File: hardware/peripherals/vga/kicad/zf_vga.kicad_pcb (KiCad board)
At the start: 2 copper layers, 33 parts, among them J2 Conn_02x13_Odd_Even, J3 DB15_Female, J4 DB9_Male, J5 DB9_Male, SW1 SW_DIP_x03, U1 4040, U10 74HC165, U11 AS6C6264, U12 74HC541, U13 74HC541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

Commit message: Bypass caps
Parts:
- added C10: 0.1uF, Capacitor_THT:C_Disc_D7.5mm_W2.5mm_P5.00mm, F.Cu at (149.9, 116.8)
- added C11: 0.1uF, Capacitor_THT:C_Disc_D7.5mm_W2.5mm_P5.00mm, F.Cu at (162.6, 82.5)
- added C12: 0.1uF, Capacitor_THT:C_Disc_D7.5mm_W2.5mm_P5.00mm, F.Cu at (149.9, 82.5)
- added C13: 0.1uF, Capacitor_THT:C_Disc_D7.5mm_W2.5mm_P5.00mm, F.Cu at (137.2, 74.9)
- added C14: 0.1uF, Capacitor_THT:C_Disc_D7.5mm_W2.5mm_P5.00mm, F.Cu at (124.5, 116.8)
- added C15: 0.1uF, Capacitor_THT:C_Disc_D7.5mm_W2.5mm_P5.00mm, F.Cu at (111.8, 116.8)
- added C16: 0.1uF, Capacitor_THT:C_Disc_D7.5mm_W2.5mm_P5.00mm, F.Cu at (104.1, 92.7)
- added C17: 0.1uF, Capacitor_THT:C_Disc_D7.5mm_W2.5mm_P5.00mm, F.Cu at (120.7, 92.7)
- added C18: 0.1uF, Capacitor_THT:C_Disc_D7.5mm_W2.5mm_P5.00mm, F.Cu at (200.7, 82.5)
- added C19: 0.1uF, Capacitor_THT:C_Disc_D7.5mm_W2.5mm_P5.00mm, F.Cu at (188.0, 82.5)
- added C20: 0.1uF, Capacitor_THT:C_Disc_D7.5mm_W2.5mm_P5.00mm, F.Cu at (175.3, 82.5)
- added C6: 0.1uF, Capacitor_THT:C_Disc_D7.5mm_W2.5mm_P5.00mm, F.Cu at (201.9, 116.8)
- added C7: 0.1uF, Capacitor_THT:C_Disc_D7.5mm_W2.5mm_P5.00mm, F.Cu at (188.0, 116.8)
- added C8: 0.1uF, Capacitor_THT:C_Disc_D7.5mm_W2.5mm_P5.00mm, F.Cu at (162.6, 116.8)
- added C9: 0.1uF, Capacitor_THT:C_Disc_D7.5mm_W2.5mm_P5.00mm, F.Cu at (175.3, 116.8)
- SW1: footprint Button_Switch_THT:SW_DIP_SPSTx03_Slide_6.7x9.18mm_W7.62mm_P2.54mm_LowProfile -> Package_DIP:DIP-6_W7.62mm_LongPads
- U1, U10, U2: footprint Package_DIP:DIP-16_W7.62mm -> Package_DIP:DIP-16_W7.62mm_LongPads
- U11: footprint Package_DIP:DIP-28_W15.24mm -> Package_DIP:DIP-28_W15.24mm_LongPads
- U12, U13, U14, U3, U4, U5, U6: footprint Package_DIP:DIP-20_W7.62mm -> Package_DIP:DIP-20_W7.62mm_LongPads
- U7, U8, U9: footprint Package_DIP:DIP-14_W7.62mm -> Package_DIP:DIP-14_W7.62mm_LongPads
- X1: footprint Oscillator:Oscillator_DIP-14 -> Oscillator:Oscillator_DIP-14_LargePads
- moved U7 59.2 mm to (143.5, 71.1)
- moved U2 47.1 mm to (168.9, 113.0)
- moved C1 45.0 mm to (142.2, 116.8)
- moved C2 44.7 mm to (142.2, 110.5)
- moved C3 44.7 mm to (142.2, 105.4)
- moved R1 43.7 mm to (143.5, 100.3)
- moved R2 43.4 mm to (143.5, 95.2)
- moved R3 43.4 mm to (143.5, 90.2)
- moved J4 38.3 mm to (154.9, 123.2)
- moved J5 37.0 mm to (189.2, 123.2)
- moved C4 36.4 mm to (91.4, 81.3), turned to 0 degrees
- moved U1 34.5 mm to (194.3, 113.0)
- moved R7 32.5 mm to (97.8, 86.4), turned to 180 degrees
- moved U9 29.5 mm to (118.1, 113.0)
- moved U8 29.2 mm to (130.8, 113.0)
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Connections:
- C4 pad 1: GND -> Net-(C4-Pad1)
- C4 pad 2: Net-(C4-Pad2) -> GND
- C5 pad 1: GND -> Net-(C5-Pad1)
- C5 pad 2: Net-(C4-Pad2) -> GND
- J3 pad 13: Net-(J3-Pad13) -> Net-(C4-Pad1)
- J3 pad 14: Net-(C4-Pad2) -> Net-(C5-Pad1)
- R7 pad 2: Net-(J3-Pad13) -> Net-(C4-Pad1)
- R8 pad 2: Net-(C4-Pad2) -> Net-(C5-Pad1)
- U12 pad 11: D7 -> D0
- U12 pad 12: D6 -> D1
- U12 pad 13: D5 -> D2
- U12 pad 14: D4 -> D3
- U12 pad 15: D3 -> D4
- U12 pad 16: D2 -> D5
- U12 pad 17: D1 -> D6
- U12 pad 18: D0 -> D7
- U12 pad 2: PA0 -> PA7
- U12 pad 3: PA1 -> PA6
- U12 pad 4: PA2 -> PA5
- U12 pad 5: PA3 -> PA4
- U12 pad 6: PA4 -> PA3
- U12 pad 7: PA5 -> PA2
- U12 pad 8: PA6 -> PA1
- U12 pad 9: PA7 -> PA0
- U13 pad 11: A7 -> A0
- U13 pad 12: A6 -> A1
- U13 pad 13: A5 -> A2
- U13 pad 14: A4 -> A3
- U13 pad 15: A3 -> A4
- U13 pad 16: A2 -> A5
- U13 pad 17: A1 -> A6
- U13 pad 18: A0 -> A7
- U13 pad 2: PB0 -> PB7
- U13 pad 3: PB1 -> PB6
- U13 pad 4: PB2 -> PB5
- U13 pad 5: PB3 -> PB4
- U13 pad 6: PB4 -> PB3
- U13 pad 7: PB5 -> PB2
- U13 pad 8: PB6 -> PB1
- U13 pad 9: PB7 -> PB0
- U14 pad 16: A10 -> A8
- U14 pad 18: A8 -> A10
- U14 pad 2: PC0 -> PC2
- U14 pad 4: PC2 -> PC0
- U3 pad 1: P0 -> P9
- U3 pad 11: P9 -> P0
- U3 pad 2: P1 -> P8
- U3 pad 3: P2 -> P7
- U3 pad 4: P3 -> P6
- U3 pad 5: P4 -> P5
- U3 pad 6: P5 -> P4
- U3 pad 7: P6 -> P3
- U3 pad 8: P7 -> P2
- U3 pad 9: P8 -> P1
- U4 pad 1: L0 -> L9
- U4 pad 11: L9 -> L0
- U4 pad 2: L1 -> L8
- U4 pad 3: L2 -> L7
- U4 pad 4: L3 -> L6
- U4 pad 5: L4 -> L5
- U4 pad 6: L5 -> L4
- U4 pad 7: L6 -> L3
- U4 pad 8: L7 -> L2
- U4 pad 9: L8 -> L1
- U5 pad 15: A3 -> A0
- U5 pad 16: A2 -> A1
- U5 pad 17: A1 -> A2
- U5 pad 18: A0 -> A3
- U5 pad 2: P5 -> P8
- U5 pad 3: P6 -> P7
- U5 pad 4: P7 -> P6
- U5 pad 5: P8 -> P5
- U6 pad 12: A10 -> A4
- U6 pad 13: A9 -> A5
- U6 pad 14: A8 -> A6
- U6 pad 16: A6 -> A8
- U6 pad 17: A5 -> A9
- U6 pad 18: A4 -> A10
- U6 pad 2: L2 -> L8
- U6 pad 3: L3 -> L7
- U6 pad 4: L4 -> L6
- U6 pad 6: L6 -> L4
- U6 pad 7: L7 -> L3
- U6 pad 8: L8 -> L2

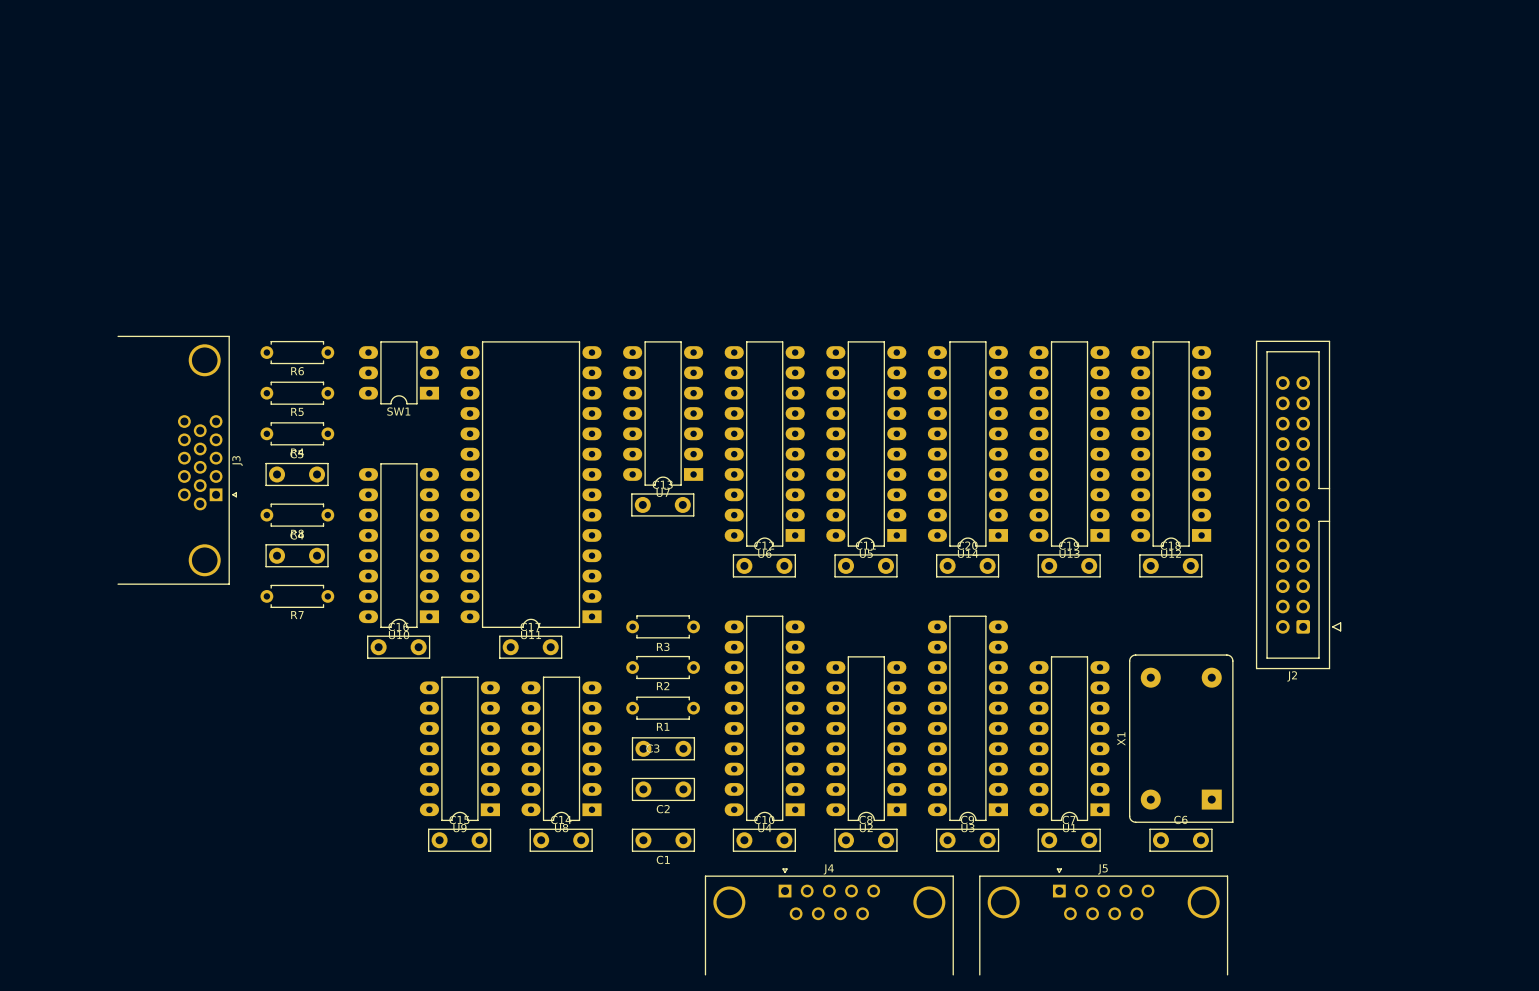
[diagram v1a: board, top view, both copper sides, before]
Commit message: Expansion port footprint
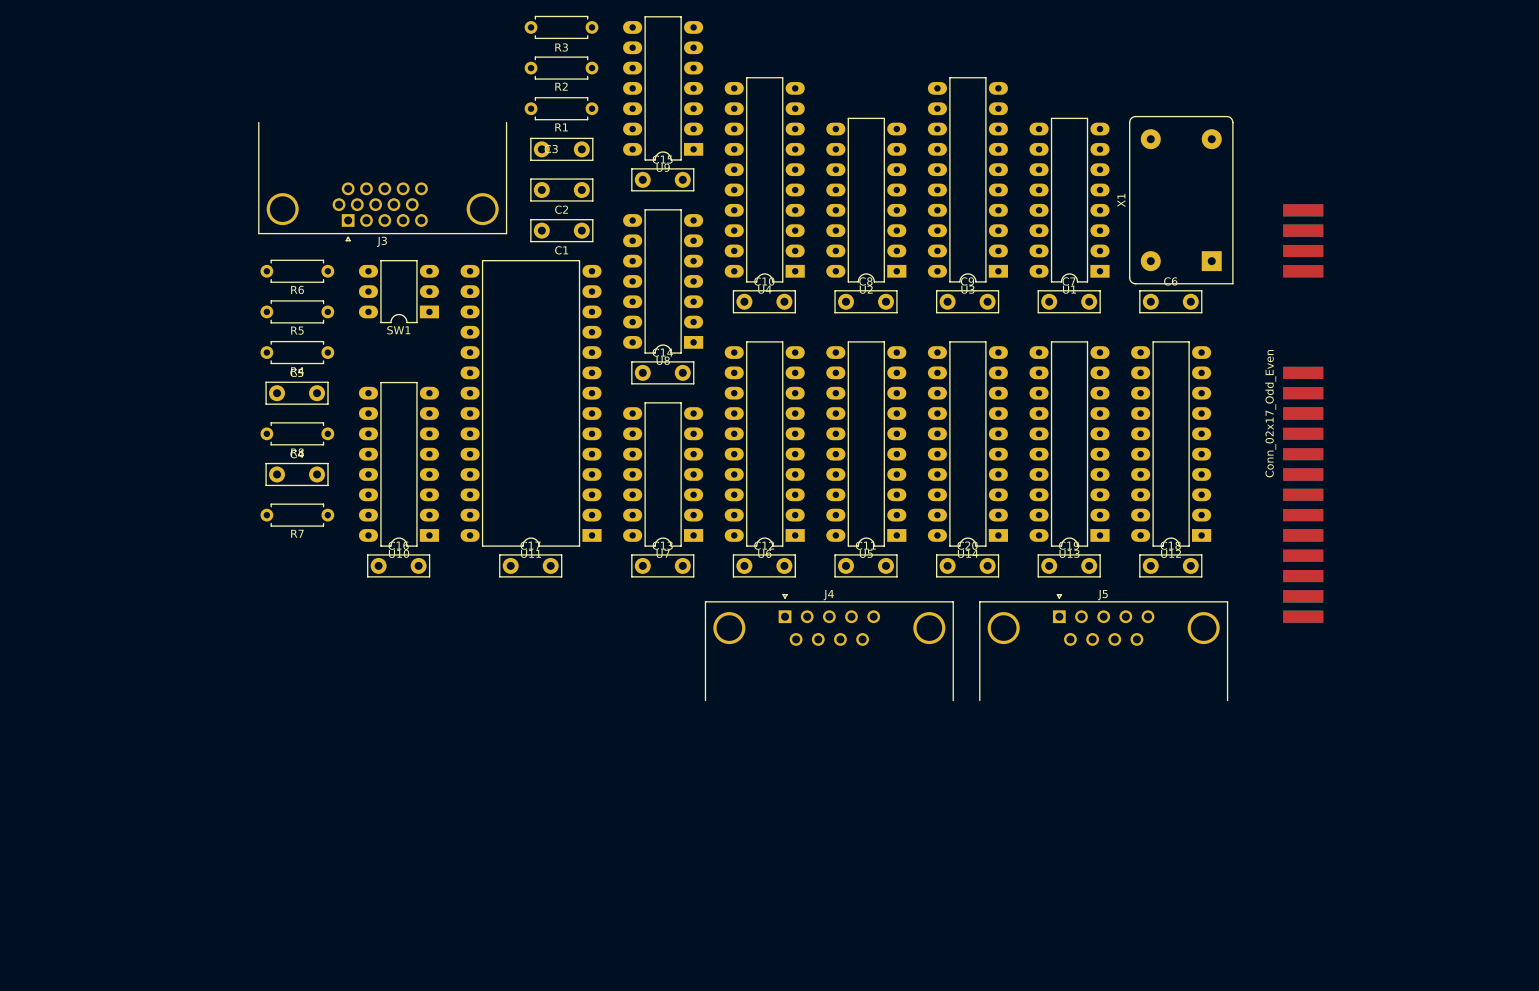
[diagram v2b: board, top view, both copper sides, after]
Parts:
- J2: value Conn_02x13_Odd_Even -> Conn_02x17_Odd_Even; footprint Connector_IDC:IDC-Header_2x13_P2.54mm_Vertical -> Z-FIGHTER:Z-FIGHTER_Expansion_Port
- moved C15 86.4 mm to (137.2, 34.3)
- moved U9 86.4 mm to (143.5, 30.5)
- moved C1 77.3 mm to (129.5, 40.6)
- moved C2 76.0 mm to (129.5, 35.6)
- moved C3 76.0 mm to (129.5, 30.5)
- moved R1 76.0 mm to (130.8, 25.4)
- moved R2 76.0 mm to (130.8, 20.3)
- moved R3 76.0 mm to (130.8, 15.2)
- moved C6 67.3 mm to (200.7, 49.5)
- moved C10 67.3 mm to (149.9, 49.5)
- moved C7 67.3 mm to (188.0, 49.5)
- moved C8 67.3 mm to (162.6, 49.5)
- moved C9 67.3 mm to (175.3, 49.5)
- moved U1 67.3 mm to (194.3, 45.7)
- moved U2 67.3 mm to (168.9, 45.7)
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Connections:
- net Net-(SW1-Pad1) renamed VIDOUT

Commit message: Board layout progress
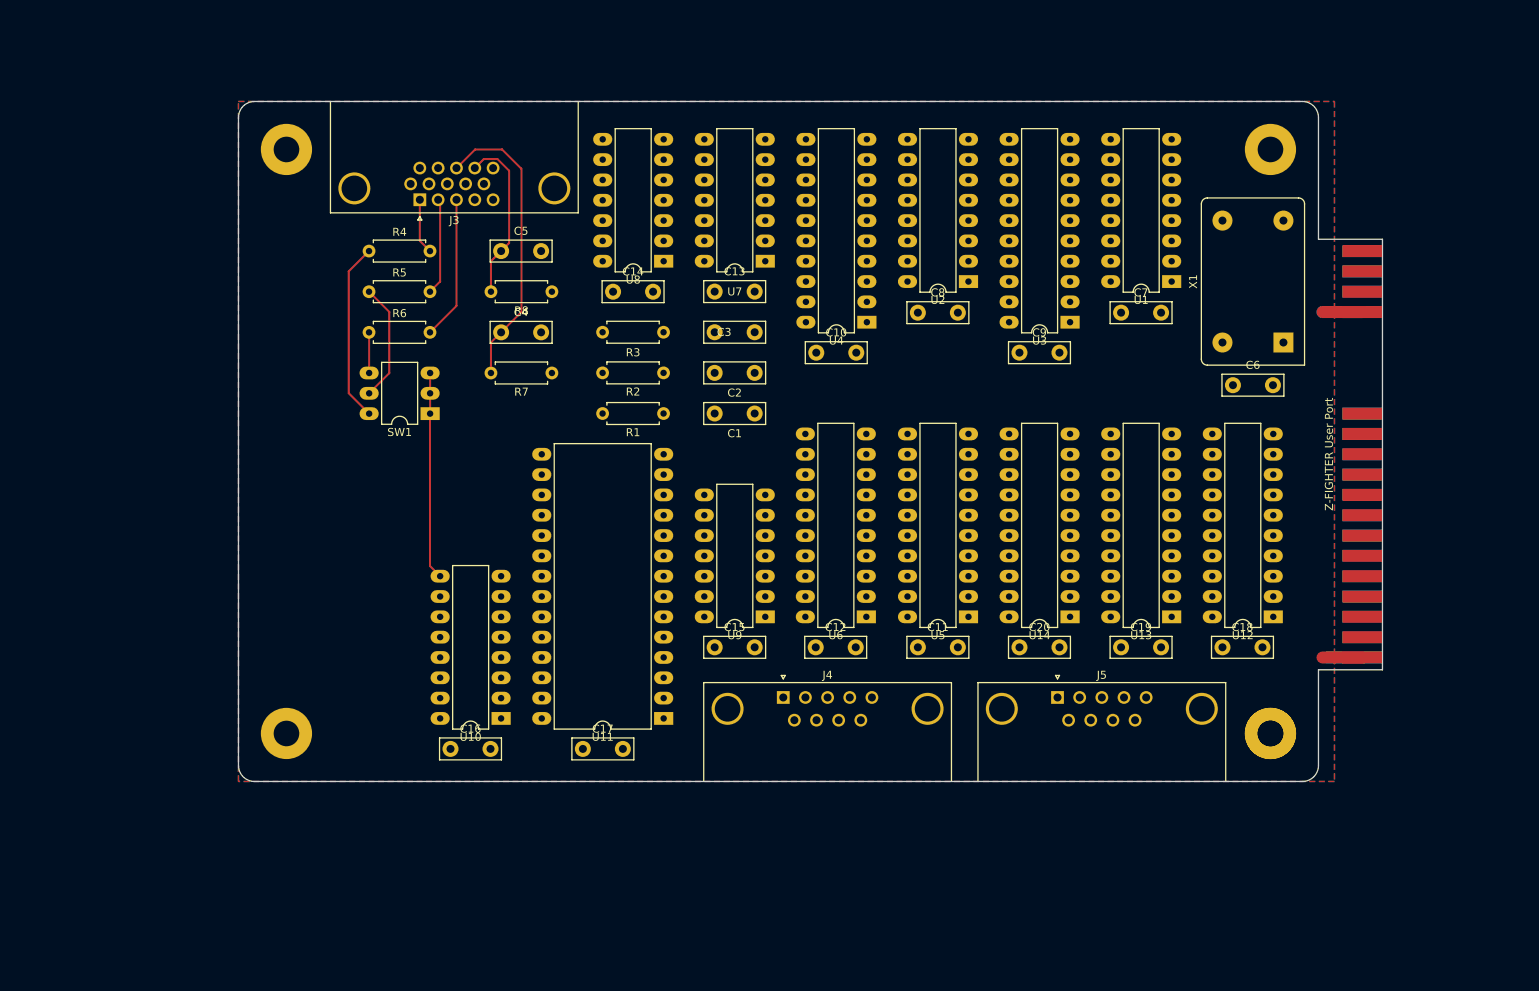
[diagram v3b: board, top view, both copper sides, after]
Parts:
- added Mount1: MountingHole_3.2mm_M3_Pad, MountingHole:MountingHole_3.2mm_M3_Pad, F.Cu at (92.6, 30.5)
- added Mount1: MountingHole_3.2mm_M3_Pad, MountingHole:MountingHole_3.2mm_M3_Pad, F.Cu at (215.6, 30.5)
- added Mount3: MountingHole_3.2mm_M3_Pad, MountingHole:MountingHole_3.2mm_M3_Pad, F.Cu at (92.6, 103.5)
- added Mount4 (x2): MountingHole_3.2mm_M3_Pad, MountingHole:MountingHole_3.2mm_M3_Pad, F.Cu at (215.6, 103.5)
- J2: value Conn_02x17_Odd_Even -> Z-FIGHTER User Port
- moved C15 59.1 mm to (146.1, 92.7)
- moved U9 59.1 mm to (152.5, 88.9)
- moved R1 39.1 mm to (139.8, 63.5)
- moved R2 39.1 mm to (139.8, 58.4)
- moved R3 39.1 mm to (139.8, 53.3)
- moved C13 35.4 mm to (146.1, 48.3)
- moved U7 35.4 mm to (152.5, 44.5)
- moved C4 33.2 mm to (119.4, 53.4)
- moved C5 33.2 mm to (119.4, 43.2)
- moved R7 33.2 mm to (125.8, 58.4)
- moved R8 33.2 mm to (125.8, 48.3)
- moved C1 31.5 mm to (151.1, 63.5)
- moved C2 31.5 mm to (151.1, 58.4)
- moved C3 31.5 mm to (151.1, 53.3)
- moved C17 24.6 mm to (129.7, 105.4)
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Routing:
- net Net-(C4-Pad1): track 0.00 -> 37.2 mm
- net VIDOUT: track 0.00 -> 25.9 mm
- net Net-(R4-Pad1): track 0.00 -> 22.4 mm
- net Net-(C5-Pad1): track 0.00 -> 21.4 mm
- net Net-(J3-Pad3): track 0.00 -> 17.9 mm
- net Net-(R5-Pad1): track 0.00 -> 14.8 mm
- net Net-(J3-Pad2): track 0.00 -> 12.1 mm
- net GND: track 0.00 -> 10.0 mm
- net VCC: track 0.00 -> 9.50 mm
- net Net-(J3-Pad1): track 0.00 -> 6.94 mm
- net Net-(R6-Pad1): track 0.00 -> 5.09 mm
- added copper zone on F.Cu, net GND
- added copper zone on B.Cu, net VCC
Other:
- board outline added: 143 x 85 mm

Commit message: Connected #RESET from ZF
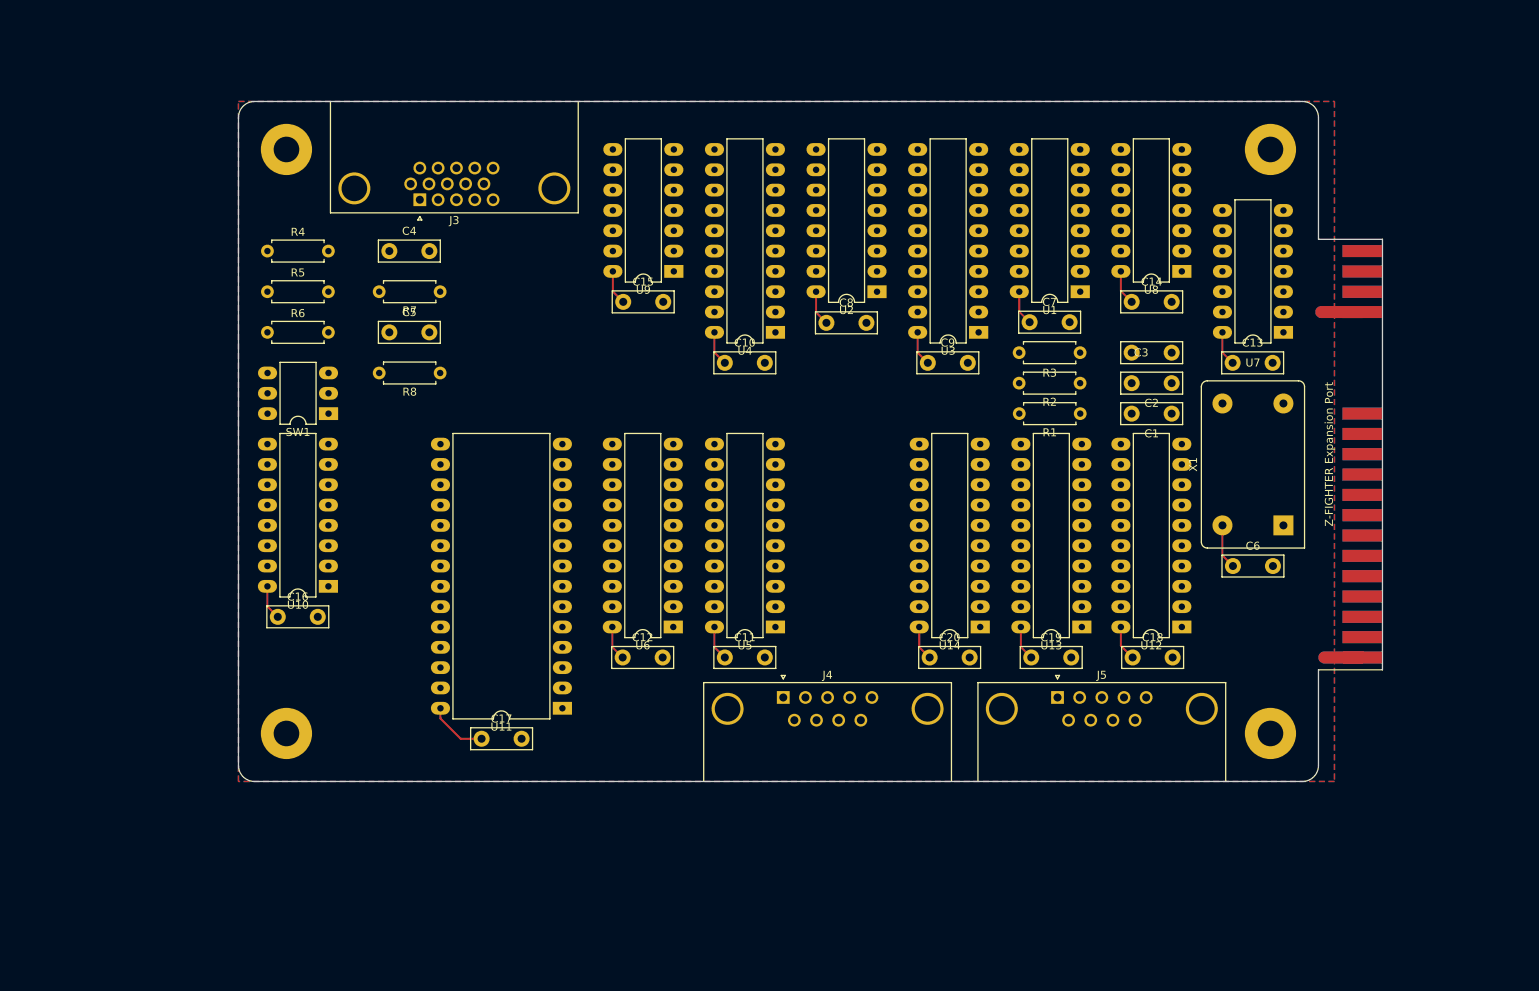
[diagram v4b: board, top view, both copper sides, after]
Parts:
- removed the Mount4 at (215.6, 103.5)
- J2: value Z-FIGHTER User Port -> Z-FIGHTER Expansion Port
- moved U7 65.4 mm to (217.2, 53.4)
- moved C13 65.4 mm to (210.9, 57.2)
- moved C14 64.8 mm to (198.3, 49.5)
- moved U8 64.8 mm to (204.5, 45.7)
- moved C3 52.2 mm to (203.3, 55.9)
- moved C2 52.1 mm to (203.3, 59.7)
- moved R3 52.1 mm to (191.8, 55.9)
- moved C1 52.1 mm to (203.3, 63.5)
- moved R2 52.1 mm to (191.8, 59.7)
- moved R1 52.1 mm to (191.8, 63.5)
- moved C15 44.7 mm to (134.7, 49.5)
- moved U9 44.7 mm to (141.0, 45.7)
- moved C16 27.2 mm to (91.5, 88.9)
- moved U10 27.2 mm to (97.9, 85.1)
- moved C11 24.2 mm to (147.4, 94.0)
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- renumbered Mount1 to Mount2
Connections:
- J2 pad 34: Net-(J2-Pad34) -> #RESET
- U13 pad 15: A4 -> A7
- U13 pad 16: A5 -> A6
- U13 pad 17: A6 -> A5
- U13 pad 18: A7 -> A4
- U13 pad 2: PB7 -> PB4
- U13 pad 3: PB6 -> PB5
- U13 pad 4: PB5 -> PB6
- U13 pad 5: PB4 -> PB7
- U3 pad 13: Net-(U3-Pad13) -> #RESET
- U4 pad 12: P4 -> Net-(U4-Pad12)
- U4 pad 13: P5 -> P4
- U4 pad 14: P9 -> P5
- U4 pad 15: Net-(U4-Pad15) -> P9
- U4 pad 16: Net-(U4-Pad16) -> #RESET
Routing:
- net VCC: track 9.50 -> 79.7 mm
- net Net-(C4-Pad1): track 37.2 -> 0.00 mm
- net VIDOUT: track 25.9 -> 0.00 mm
- net Net-(R4-Pad1): track 22.4 -> 0.00 mm
- net Net-(C5-Pad1): track 21.4 -> 0.00 mm
- net Net-(J3-Pad3): track 17.9 -> 0.00 mm
- net Net-(R5-Pad1): track 14.8 -> 0.00 mm
- net Net-(J3-Pad2): track 12.1 -> 0.00 mm
- net Net-(J3-Pad1): track 6.94 -> 0.00 mm
- net Net-(R6-Pad1): track 5.09 -> 0.00 mm
